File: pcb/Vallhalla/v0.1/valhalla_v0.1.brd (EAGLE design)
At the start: 88.9 x 53 mm, 15 parts, among them J1 POWER_JACKPTH, U1 LM317, U2 TLC5940-NT

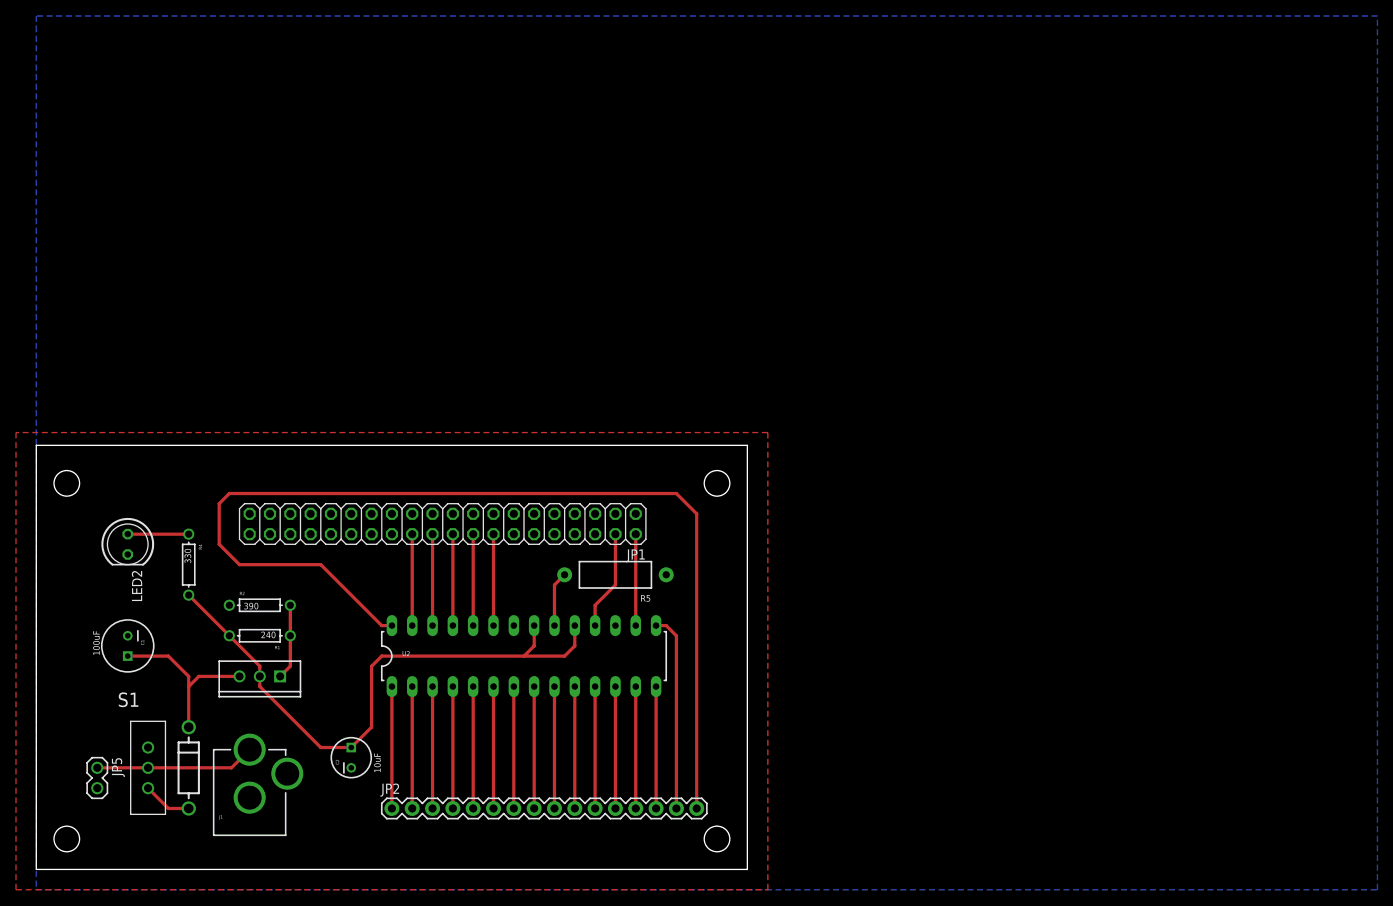
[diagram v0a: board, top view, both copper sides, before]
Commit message: Misc changes based on availability of components
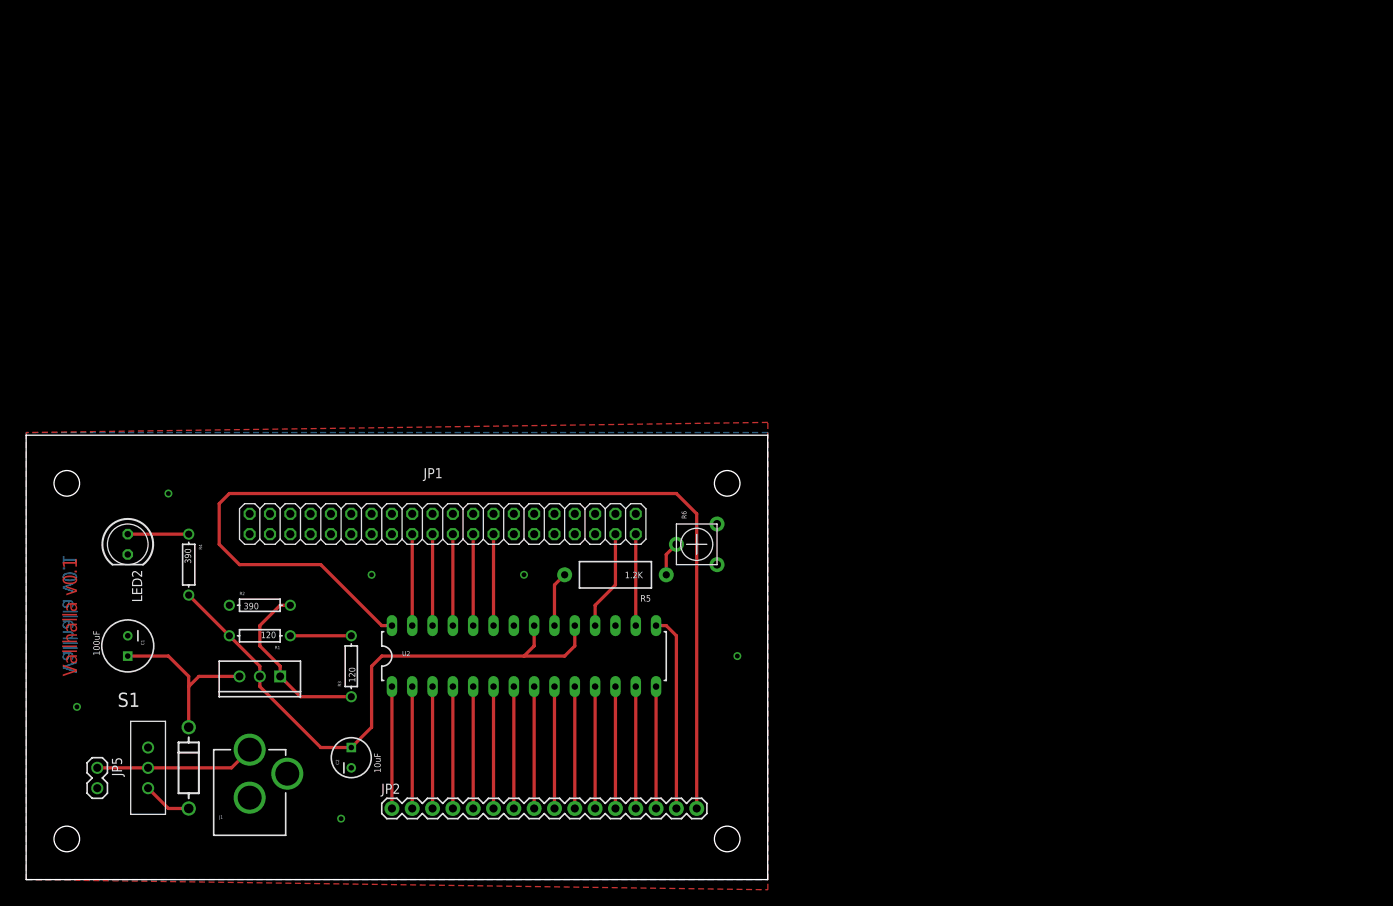
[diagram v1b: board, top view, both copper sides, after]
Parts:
- added R3: 120, SparkFun:AXIAL-0.3
- added R6: TRIMPOTPTH, SparkFun-Electromechanical:TRIM_POT_PTH
- R1: value 240 -> 120
- R4: value 330 -> 390
- R5: value (none) -> 1.2K
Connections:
- new net N$22: R1.P$1, R3.P$2
- new net N$24: R2.P$2, R3.P$1, U1.ADJ
- net GND: now also R6.1; no longer R5.P$1
- net N$5: now also R5.P$1, R6.2; no longer R1.P$1, R2.P$2, U1.ADJ
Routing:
- net N$24: track 0.00 -> 22.2 mm
- net N$22: track 0.00 -> 7.62 mm
- net N$5: track 9.42 -> 4.34 mm
- added copper zone on layer 1, net GND
- removed copper zone on layer 1, net N$21
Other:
- board size 88.9 x 53 mm -> 92.7 x 55.5 mm
- board text added: "Vallhalla v0.1"
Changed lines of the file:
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@@
 <board>
 <plain>
-<wire x1="-3.81" y1="-3.81" x2="85.07" y2="-3.81" width="0" layer="20"/>
-<wire x1="85.07" y1="-3.81" x2="85.07" y2="49.2" width="0" layer="20"/>
-<wire x1="85.07" y1="49.2" x2="-3.81" y2="49.2" width="0" layer="20"/>
-<wire x1="-3.81" y1="49.2" x2="-3.81" y2="-3.81" width="0" layer="20"/>
+<wire x1="-5.08" y1="-5.08" x2="87.61" y2="-5.08" width="0" layer="20"/>
+<wire x1="87.61" y1="-5.08" x2="87.61" y2="50.47" width="0" layer="20"/>
+<wire x1="87.61" y1="50.47" x2="-5.08" y2="50.47" width="0" layer="20"/>
+<wire x1="-5.08" y1="50.47" x2="-5.08" y2="-5.08" width="0" layer="20"/>
 <hole x="0" y="44.45" drill="3.2"/>
-<hole x="81.28" y="44.45" drill="3.2"/>
-<hole x="81.28" y="0" drill="3.2"/>
+<hole x="82.55" y="44.45" drill="3.2"/>
+<hole x="82.55" y="0" drill="3.2"/>
 <hole x="0" y="0" drill="3.2"/>
+<text x="1.27" y="20.32" size="1.778" layer="1" rot="R90">Vallhalla v0.1</text>
+<text x="1.27" y="35.56" size="1.778" layer="16" rot="MR270">Vallhalla v0.1</text>
 </plain>
 <attributes>
@@
 <element name="R2" library="SparkFun" package="AXIAL-0.3" value="390" x="24.13" y="29.21"/>
 <element name="C1" library="SparkFun" package="CPOL-RADIAL-100UF-25V" value="100uF" x="7.62" y="24.13" rot="R270"/>
-<element name="R1" library="SparkFun" package="AXIAL-0.3" value="240" x="24.13" y="25.4" rot="R180"/>
-<element name="R4" library="SparkFun" package="AXIAL-0.3" value="330" x="15.24" y="34.29" rot="R270"/>
+<element name="R1" library="SparkFun" package="AXIAL-0.3" value="120" x="24.13" y="25.4" rot="R180"/>
+<element name="R4" library="SparkFun" package="AXIAL-0.3" value="390" x="15.24" y="34.29" rot="R270"/>
 <element name="C2" library="SparkFun" package="CPOL-RADIAL-10UF-25V" value="10uF" x="35.56" y="10.16" rot="R90"/>
 <element name="LED2" library="SparkFun-Nate" package="LED5MM" value="Power" x="7.62" y="36.83" rot="R270"/>
@@
 <element name="D1" library="SparkFun" package="DIODE-0.4" value="1N4001" x="15.24" y="3.81" rot="R90"/>
 <element name="U2" library="SparkFun-DigitalIC" package="DIL28-3" value="TLC5940-NT" x="57.15" y="22.86"/>
-<element name="JP1" library="adafruit" package="2X20" value="" x="46.99" y="39.37" rot="R180"/>
+<element name="JP1" library="adafruit" package="2X20" value="" x="46.99" y="39.37" smashed="yes" rot="R180">
+<attribute name="NAME" x="46.99" y="46.355" size="1.27" layer="25" ratio="10" rot="R180"/>
+<attribute name="VALUE" x="72.39" y="43.815" size="1.27" layer="27" rot="R180"/>
+</element>
 <element name="JP2" library="SparkFun-Connectors" package="1X16" value="M16PTH" x="40.64" y="3.81"/>
-<element name="R5" library="SparkFun-Resistors" package="AXIAL-0.5" value="" x="68.58" y="33.02" rot="R180"/>
+<element name="R5" library="SparkFun-Resistors" package="AXIAL-0.5" value="1.2K" x="68.58" y="33.02" rot="R180"/>
+<element name="R3" library="SparkFun" package="AXIAL-0.3" value="120" x="35.56" y="21.59" rot="R90"/>
+<element name="R6" library="SparkFun-Electromechanical" package="TRIM_POT_PTH" value="TRIMPOTPTH" x="78.74" y="36.83" smashed="yes" rot="R90">
+<attribute name="NAME" x="77.47" y="40.005" size="0.6096" layer="25" rot="R90"/>
+<attribute name="VALUE" x="83.82" y="33.655" size="0.6096" layer="27" rot="R90"/>
+</element>
 </elements>
 <signals>
@@
 <contactref element="J1" pad="GNDBREAK"/>
 <contactref element="JP5" pad="2"/>
-<polygon width="0.6096" layer="16" isolate="0.8128">
-<vertex x="-3.81" y="101.6"/>
-<vertex x="-3.81" y="-6.35"/>
-<vertex x="163.83" y="-6.35"/>
-<vertex x="163.83" y="102.87"/>
-<vertex x="-3.81" y="102.87"/>
-</polygon>
 <contactref element="JP1" pad="12"/>
 <contactref element="JP1" pad="30"/>
 <contactref element="U2" pad="22"/>
-<contactref element="R5" pad="P$1"/>
+<polygon width="0.4064" layer="16" isolate="1.4224">
+<vertex x="-5.08" y="50.8"/>
+<vertex x="-5.08" y="-5.08"/>
+<vertex x="87.63" y="-5.08"/>
+<vertex x="87.63" y="50.8"/>
+</polygon>
+<polygon width="0.4064" layer="1" isolate="1.4224">
+<vertex x="-5.08" y="50.8"/>
+<vertex x="-5.08" y="-5.08"/>
+<vertex x="87.63" y="-6.35"/>
+<vertex x="87.63" y="52.07"/>
+</polygon>
+<via x="1.27" y="16.51" extent="1-16" drill="0.6" shape="square"/>
+<via x="12.7" y="43.18" extent="1-16" drill="0.6" shape="square"/>
+<via x="34.29" y="2.54" extent="1-16" drill="0.6" shape="square"/>
+<via x="83.82" y="22.86" extent="1-16" drill="0.6" shape="square"/>
 <contactref element="R2" pad="P$1"/>
-</signal>
-<signal name="N$5">
-<contactref element="R2" pad="P$2"/>
-<contactref element="R1" pad="P$1"/>
-<contactref element="U1" pad="ADJ"/>
-<wire x1="27.94" y1="25.4" x2="27.94" y2="21.59" width="0.4064" layer="1"/>
-<wire x1="27.94" y1="21.59" x2="26.67" y2="20.32" width="0.4064" layer="1"/>
-<wire x1="27.94" y1="25.4" x2="27.94" y2="29.21" width="0.4064" layer="1"/>
+<contactref element="R6" pad="1"/>
+<via x="38.1" y="33.02" extent="1-16" drill="0.6" shape="square"/>
+<via x="57.15" y="33.02" extent="1-16" drill="0.6" shape="square"/>
 </signal>
 <signal name="N$8">
@@
 <wire x1="43.18" y1="26.67" x2="43.18" y2="38.1" width="0.4064" layer="1"/>
 </signal>
-<signal name="N$21">
-<polygon width="0.4064" layer="1" spacing="0.8128" isolate="0.4064">
-<vertex x="-6.35" y="50.8"/>
-<vertex x="-6.35" y="-6.35"/>
-<vertex x="87.63" y="-6.35"/>
-<vertex x="87.63" y="50.8"/>
-</polygon>
+<signal name="N$22">
+<contactref element="R1" pad="P$1"/>
+<contactref element="R3" pad="P$2"/>
+<wire x1="35.56" y1="25.4" x2="27.94" y2="25.4" width="0.4064" layer="1"/>
+</signal>
+<signal name="N$24">
+<contactref element="R3" pad="P$1"/>
+<contactref element="R2" pad="P$2"/>
+<contactref element="U1" pad="ADJ"/>
+<wire x1="26.67" y1="20.32" x2="29.21" y2="17.78" width="0.4064" layer="1"/>
+<wire x1="29.21" y1="17.78" x2="35.56" y2="17.78" width="0.4064" layer="1"/>
+<wire x1="26.67" y1="20.32" x2="26.67" y2="21.59" width="0.4064" layer="1"/>
+<wire x1="26.67" y1="21.59" x2="24.13" y2="24.13" width="0.4064" layer="1"/>
+<wire x1="24.13" y1="24.13" x2="24.13" y2="26.67" width="0.4064" layer="1"/>
+<wire x1="24.13" y1="26.67" x2="26.67" y2="29.21" width="0.4064" layer="1"/>
+<wire x1="26.67" y1="29.21" x2="27.94" y2="29.21" width="0.4064" layer="1"/>
+</signal>
+<signal name="N$5">
+<contactref element="R5" pad="P$1"/>
+<contactref element="R6" pad="2"/>
+<wire x1="76.2" y1="36.83" x2="74.93" y2="35.56" width="0.4064" layer="1"/>
+<wire x1="74.93" y1="35.56" x2="74.93" y2="33.02" width="0.4064" layer="1"/>
 </signal>
 </signals>
